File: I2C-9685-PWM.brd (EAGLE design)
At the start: 106 x 100 mm, 34 parts, among them SW1 A0-A3, SW2 A4-A5

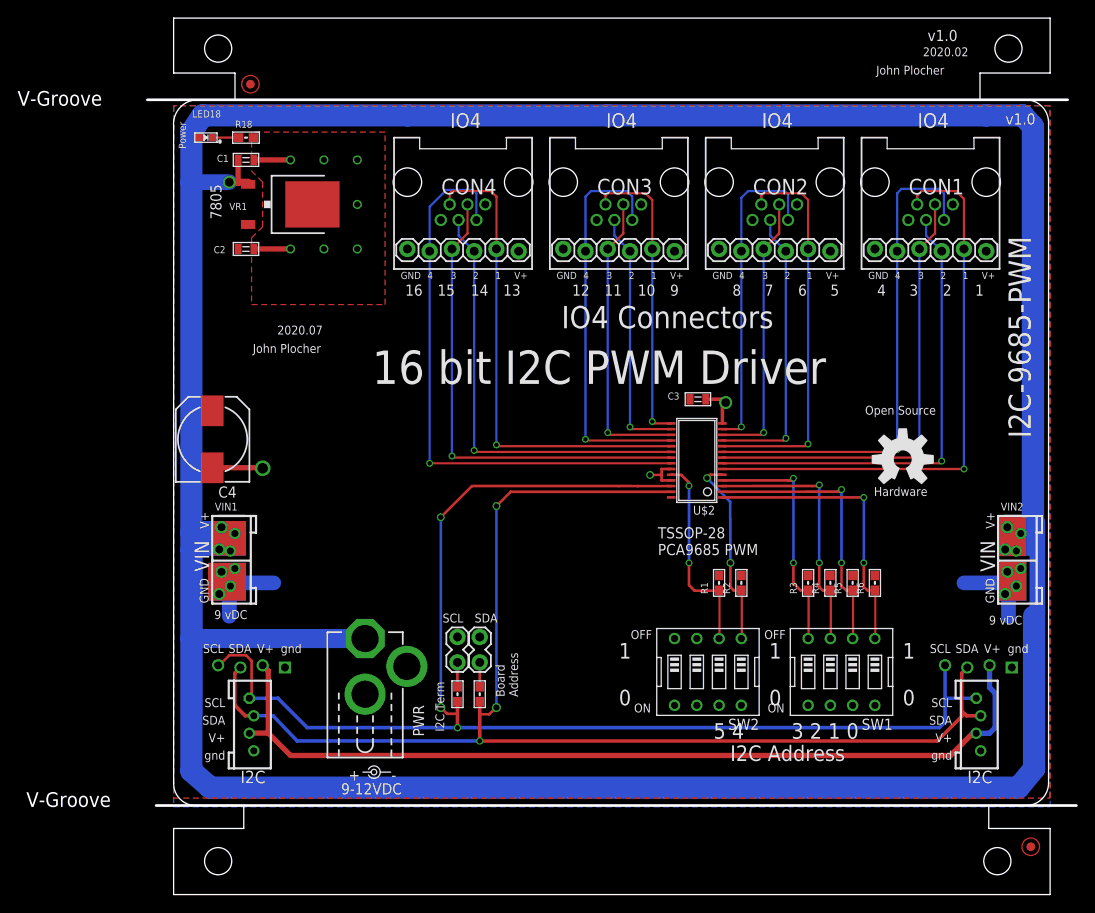
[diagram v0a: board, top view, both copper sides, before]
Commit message: RR Tracks on back silk, better ground plane
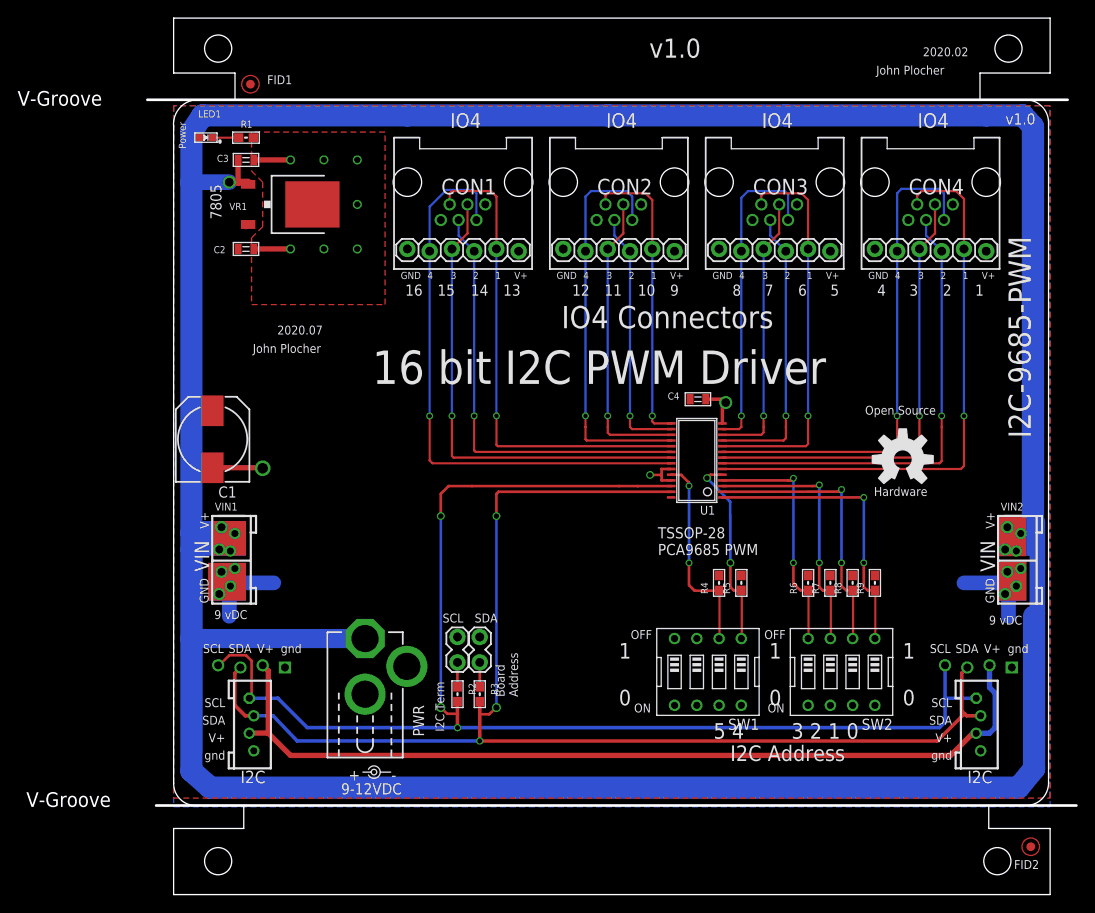
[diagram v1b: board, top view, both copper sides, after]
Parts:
- removed R18: 2K0, SPCoast:0603-RES
- removed R19, R20: 4k7, SPCoast:0603-RES
- added R7, R8, R9: 10k, SPCoast:0603-RES
- C1: value 0.1uF -> 220uF; device SPCoast:0805-CAP -> SPCoast:0810-CAP
- C4: value 220uF -> 0.1uF; device SPCoast:0810-CAP -> SPCoast:0805-CAP
- R1: value 10k -> 2K0
- R2, R3: value 10k -> 4k7
- SW1: value A0-A3 -> A4-A5
- SW2: value A4-A5 -> A0-A3
- moved J1 82.9 mm to (8.89, 26.0)
- moved J2 82.9 mm to (91.8, 26.0)
- moved R1 74.1 mm to (8.26, 86.4), turned to 0 degrees
- moved C3 58.3 mm to (8.26, 83.8)
- moved C4 55.6 mm to (59.8, 56.5), turned to 0 degrees
- moved CON1 53.3 mm to (33.0, 77.5)
- moved CON4 53.3 mm to (86.4, 77.5)
- moved R3 39.6 mm to (34.9, 22.9), turned to 270 degrees
- moved R2 34.8 mm to (32.4, 22.9), turned to 270 degrees
- moved C1 32.1 mm to (4.45, 51.9), turned to 90 degrees
- moved CON2 17.8 mm to (50.8, 77.5)
- moved CON3 17.8 mm to (68.6, 77.5)
- moved SW1 15.2 mm to (61.0, 25.4)
- moved SW2 15.2 mm to (76.2, 25.4)
- moved R4 12.7 mm to (62.2, 35.6)
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- renumbered LED18 to LED1, U$2 to U1
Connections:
- net +9V: now also C3.1; no longer C1.1
- net A0: now also R9.1, SW2.1; no longer R6.1, SW1.1
- net A1: now also R8.1, SW2.2; no longer R5.1, SW1.2
- net A2: now also R7.1, SW2.3; no longer R4.1, SW1.3
- net A3: now also R6.1, SW2.4; no longer R3.1, SW1.4
- net A4: now also R5.1, SW1.1; no longer R2.1, SW2.1
- net A5: now also R4.1, SW1.2; no longer R1.1, SW2.2
- net GND: now also C1.-, C4.2, R1.2, SW2.5, SW2.6; no longer C1.2, C4.-, R18.2, SW1.5, SW1.6
- net N$1: now also R1.1; no longer R18.1
- net N$19: now also R3.1; no longer R19.1
- net N$20: now also R2.1; no longer R20.1
- net P1: now also CON4.2, CON4.2@1; no longer CON1.2, CON1.2@1
- net P10: now also CON2.3, CON2.3@1; no longer CON3.3, CON3.3@1
- net P11: now also CON2.4, CON2.4@1; no longer CON3.4, CON3.4@1
- net P12: now also CON2.5, CON2.5@1; no longer CON3.5, CON3.5@1
- net P13: now also CON1.2, CON1.2@1; no longer CON4.2, CON4.2@1
- net P14: now also CON1.3, CON1.3@1; no longer CON4.3, CON4.3@1
- net P15: now also CON1.4, CON1.4@1; no longer CON4.4, CON4.4@1
- net P16: now also CON1.5, CON1.5@1; no longer CON4.5, CON4.5@1
- net P2: now also CON4.3, CON4.3@1; no longer CON1.3, CON1.3@1
- net P3: now also CON4.4, CON4.4@1; no longer CON1.4, CON1.4@1
- net P4: now also CON4.5, CON4.5@1; no longer CON1.5, CON1.5@1
- net P5: now also CON3.2, CON3.2@1; no longer CON2.2, CON2.2@1
- net P6: now also CON3.3, CON3.3@1; no longer CON2.3, CON2.3@1
- net P7: now also CON3.4, CON3.4@1; no longer CON2.4, CON2.4@1
- net P8: now also CON3.5, CON3.5@1; no longer CON2.5, CON2.5@1
- net P9: now also CON2.2, CON2.2@1; no longer CON3.2, CON3.2@1
- net SCL: now also R2.2; no longer R20.2
- net SDA: now also R3.2; no longer R19.2
- net VCC: now also C1.+, C4.1, R7.2, R8.2, R9.2; no longer C3.1, C4.+, R1.2, R2.2, R3.2
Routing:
- net SCL: track 154.8 -> 156.3 mm
- net SDA: track 148.8 -> 149.6 mm
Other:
- board text removed: "A "1" bit in the I/O register is associated with a LOW voltage on a pin"
- board text removed: "Active Low:"

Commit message: better spacing on IO4s and heatsinking on 7805
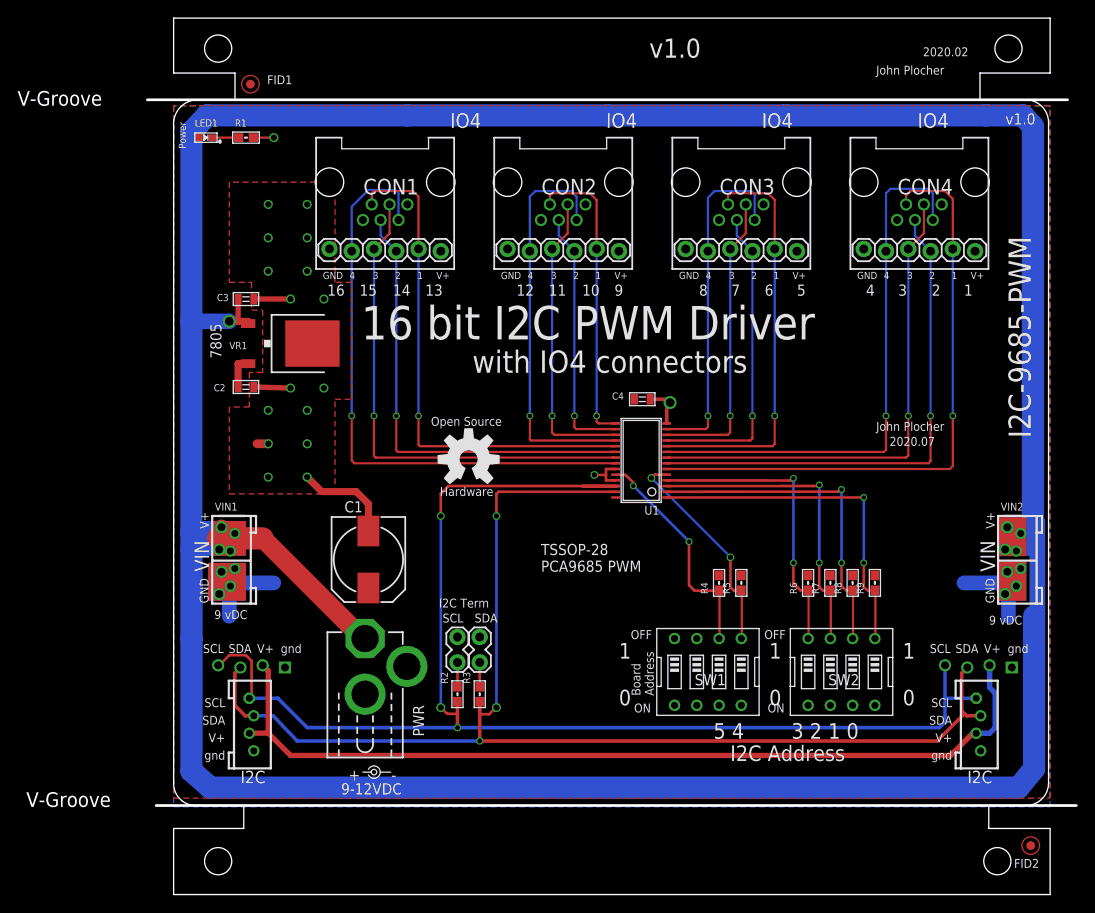
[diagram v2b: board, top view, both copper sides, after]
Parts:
- SW1: value A4-A5 -> xx xx A5 A4
- SW2: value A0-A3 -> A3 A2 A1 A0
- moved U$1 49.5 mm to (33.7, 49.7)
- moved C1 22.5 mm to (22.2, 38.2), turned to 270 degrees
- moved C3 15.9 mm to (8.26, 67.9)
- moved VR1 15.9 mm to (13.3, 62.9)
- moved C2 15.7 mm to (8.26, 57.9)
- moved CON1 8.89 mm to (24.1, 77.5)
- moved C4 6.35 mm to (53.5, 56.5)
- moved CON2 6.35 mm to (44.5, 77.5)
- moved U1 6.35 mm to (53.3, 49.5)
- moved CON3 3.81 mm to (64.8, 77.5)
- moved CON4 1.27 mm to (85.1, 77.5)
- moved FID2 0.13 mm to (97.8, 5.59)
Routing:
- net GND: track 51.0 -> 60.2 mm, vias 10 -> 19
- net SDA: track 149.6 -> 143.2 mm
- net A0: track 33.3 -> 39.7 mm
- net A2: track 29.7 -> 36.0 mm
- net A3: track 27.8 -> 34.2 mm
- net A1: track 31.7 -> 38.1 mm
- net P2: track 53.4 -> 58.4 mm
- net P4: track 58.1 -> 63.2 mm
- net P3: track 52.0 -> 57.0 mm
- net P1: track 65.1 -> 70.2 mm
- net VCC: track 0.36 -> 4.18 mm
- net +9V: track 406.7 -> 409.6 mm
- net A4: track 22.3 -> 24.9 mm
- net A5: track 23.3 -> 25.9 mm
- net P6: track 33.0 -> 35.5 mm
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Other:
- board text added: "with IO4 connectors"
- board text removed: "IO4 Connectors"

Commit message: fixed SPCoast lbr part orientation
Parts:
- R1: value 2K0 -> 4k7
- turned LED1 to 180 degrees
- turned VR1 to 0 degrees
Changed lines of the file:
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@@
 <setting verticaltext="up"/>
 </settings>
-<grid distance="50" unitdist="mil" unit="mil" style="dots" multiple="2" display="yes" altdistance="5" altunitdist="mil" altunit="mil"/>
+<grid distance="50" unitdist="mil" unit="mil" style="dots" multiple="2" display="yes" altdistance="25" altunitdist="mil" altunit="mil"/>
 <layers>
 <layer number="1" name="Top" color="4" fill="1" visible="yes" active="yes"/>
@@
 </element>
 <element name="U$1" library="SparkFun" package="OSHW-LOGO-L" value="OSHW-LOGOL" x="33.655" y="49.657" smashed="yes"/>
-<element name="VR1" library="SPCoast" package="TO-252" value="CJ7805" x="13.335" y="62.865" smashed="yes" rot="R270">
-<attribute name="NAME" x="6.35" y="62.23" size="0.8128" layer="25" ratio="11"/>
-</element>
-<element name="R1" library="SPCoast" package="0603-RES" value="2K0" x="8.255" y="86.36" smashed="yes">
+<element name="VR1" library="SPCoast" package="TO-252" value="CJ7805" x="13.335" y="62.865" smashed="yes">
+<attribute name="NAME" x="13.97" y="55.88" size="0.8128" layer="25" ratio="11" rot="R90"/>
+</element>
+<element name="R1" library="SPCoast" package="0603-RES" value="4k7" x="8.255" y="86.36" smashed="yes">
 <attribute name="PROD_ID" value="RES-08272" x="8.255" y="86.36" size="0.8128" layer="27" display="off"/>
 <attribute name="NAME" x="6.985" y="87.63" size="0.8128" layer="25" font="vector"/>
 <attribute name="VALUE" x="6.985" y="84.455" size="0.8128" layer="27" font="vector"/>
 </element>
-<element name="LED1" library="SPCoast" package="0603-LED" value="G" x="3.683" y="86.36" smashed="yes">
-<attribute name="NAME" x="2.413" y="87.63" size="0.8128" layer="25"/>
-<attribute name="VALUE" x="3.556" y="84.455" size="0.8128" layer="27"/>
+<element name="LED1" library="SPCoast" package="0603-LED" value="G" x="3.683" y="86.36" smashed="yes" rot="R180">
+<attribute name="NAME" x="4.953" y="85.09" size="0.8128" layer="25" rot="R180"/>
+<attribute name="VALUE" x="3.81" y="88.265" size="0.8128" layer="27" rot="R180"/>
 </element>
 <element name="J2" library="SPCoast" package="I2C-L" value="" x="91.821" y="26.035" smashed="yes"/>
@@
 <vertex x="18.415" y="45.72"/>
 <vertex x="18.415" y="56.515"/>
-<vertex x="20.32" y="56.515"/>
-<vertex x="20.32" y="69.85"/>
+<vertex x="30.48" y="56.515"/>
+<vertex x="30.48" y="69.85"/>
 <vertex x="18.415" y="69.85"/>
 <vertex x="18.415" y="81.28"/>

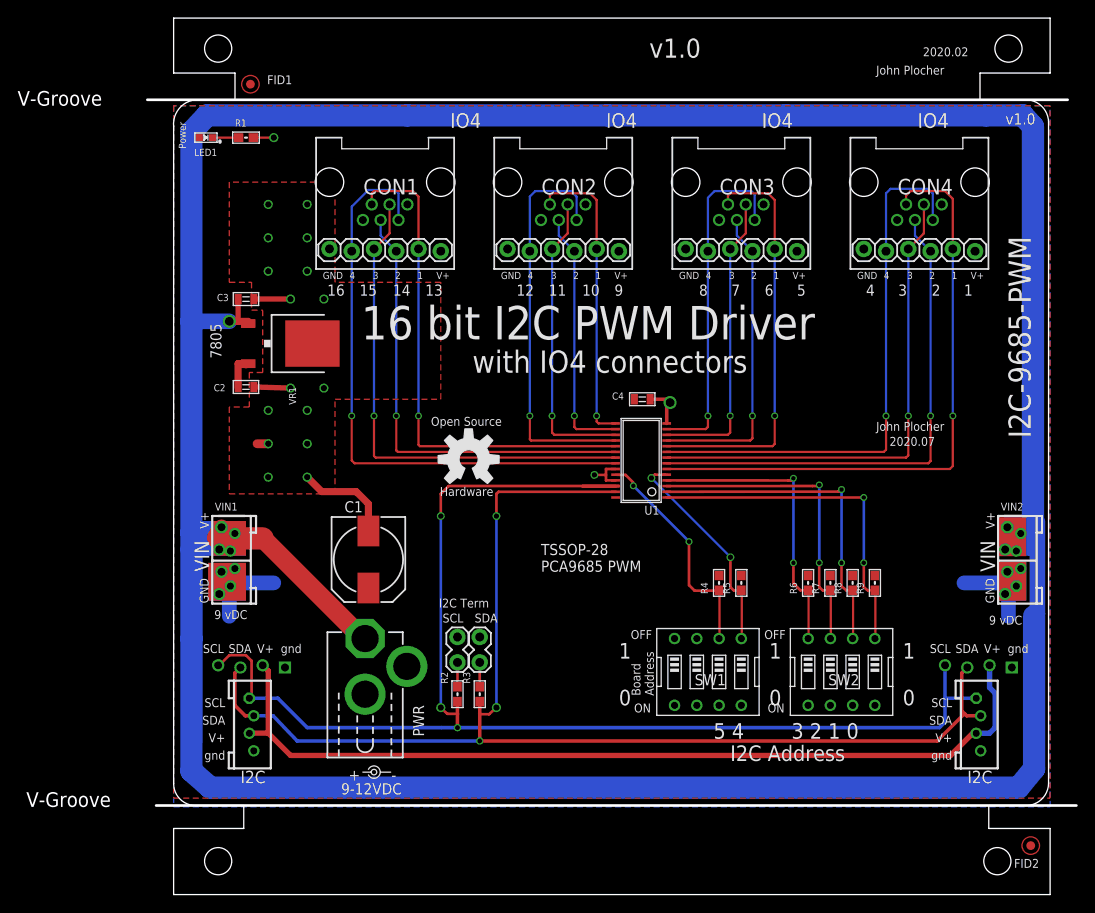
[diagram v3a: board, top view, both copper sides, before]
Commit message: FID placement & names
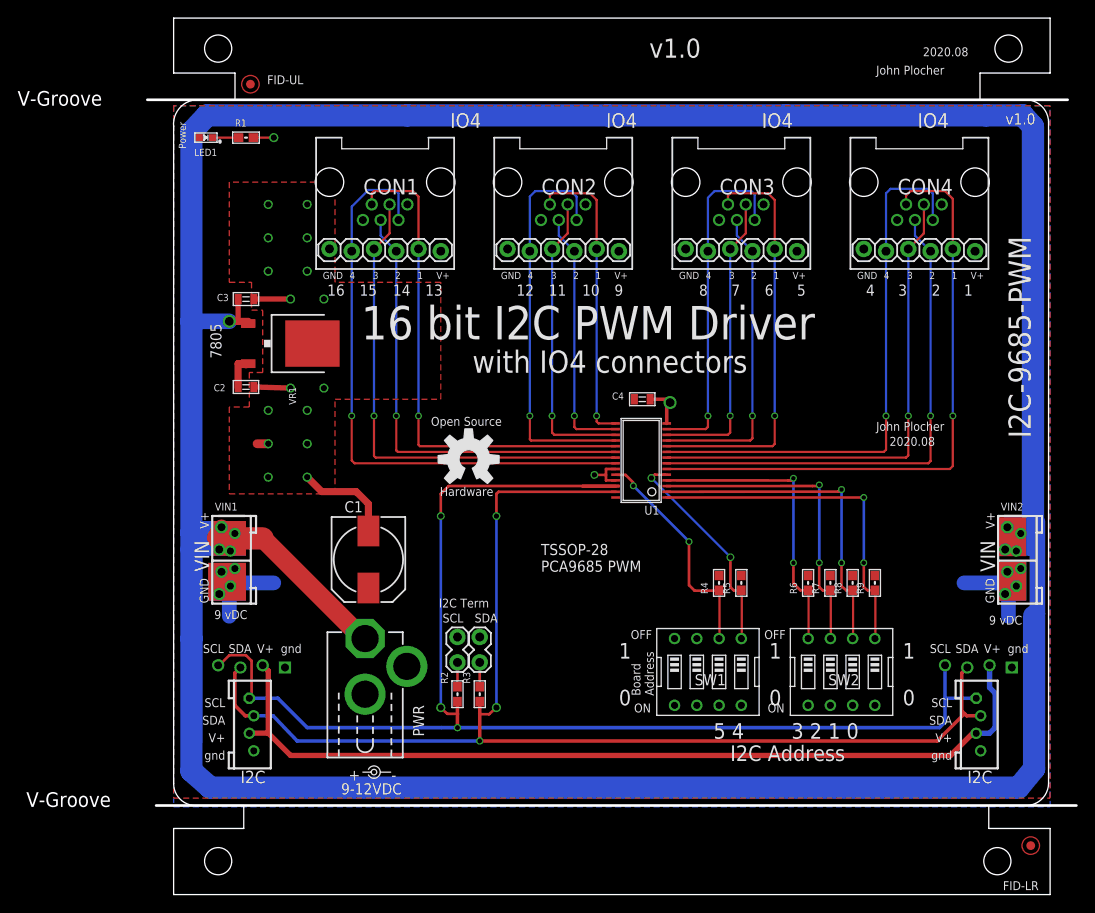
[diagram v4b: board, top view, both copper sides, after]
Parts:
- renumbered FID1 to FID-UL, FID2 to FID-LR
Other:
- board text added: "2020.08"
- board text removed: "2020.02"
- board text removed: "2020.07"
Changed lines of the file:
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@@
 <text x="1.397" y="85.09" size="0.8128" layer="21" rot="R90">Power</text>
 <text x="54.26339375" y="95.475534375" size="2.1844" layer="21" ratio="10" rot="SR0">v1.0</text>
-<text x="85.48799375" y="95.645009375" size="1.016" layer="21">2020.02</text>
-<text x="81.67799375" y="51.195009375" size="1.016" layer="21">2020.07</text>
+<text x="85.48799375" y="95.645009375" size="1.016" layer="21">2020.08</text>
+<text x="81.67799375" y="51.195009375" size="1.016" layer="21">2020.08</text>
 <text x="90.17" y="68.326" size="1.27" layer="21">1</text>
 <text x="86.487" y="68.326" size="1.27" layer="21">2</text>
@@
 <element name="J1" library="SPCoast" package="I2C-L" value="" x="8.89" y="26.035" smashed="yes"/>
 <element name="BOARD1" library="SPCoast" package="BOARD-DINRAIL-3.17IN-IOB" value="BOARD80X100-IOB" x="0" y="0"/>
-<element name="FID1" library="SPCoast" package="FIDUCIAL_1MM" value="FIDUCIAL" x="8.763" y="92.456" smashed="yes">
+<element name="FID-UL" library="SPCoast" package="FIDUCIAL_1MM" value="FIDUCIAL" x="8.763" y="92.456" smashed="yes">
 <attribute name="NAME" x="10.668" y="92.456" size="1.016" layer="25"/>
 </element>
-<element name="FID2" library="SPCoast" package="FIDUCIAL_1MM" value="FIDUCIAL" x="97.79" y="5.588"/>
+<element name="FID-LR" library="SPCoast" package="FIDUCIAL_1MM" value="FIDUCIAL" x="97.79" y="5.588" smashed="yes">
+<attribute name="NAME" x="94.615" y="0.508" size="1.016" layer="25"/>
+</element>
 <element name="SW2" library="SPCoast" package="EDG-04" value="A3 A2 A1 A0" x="76.2" y="25.4" smashed="yes" rot="R180">
 <attribute name="VALUE" x="82.042" y="32.004" size="1.016" layer="27" ratio="10" rot="R180"/>
